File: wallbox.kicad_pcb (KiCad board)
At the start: 2 copper layers, 48 parts, among them J1 From Transformer, J2 To Wallbox, J3 UART, J4 Program, Q1 BC547, Q2 BC547, Q3 BC547, SW1 SW_Push, U1 KA78R33, U2 LM7805CT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

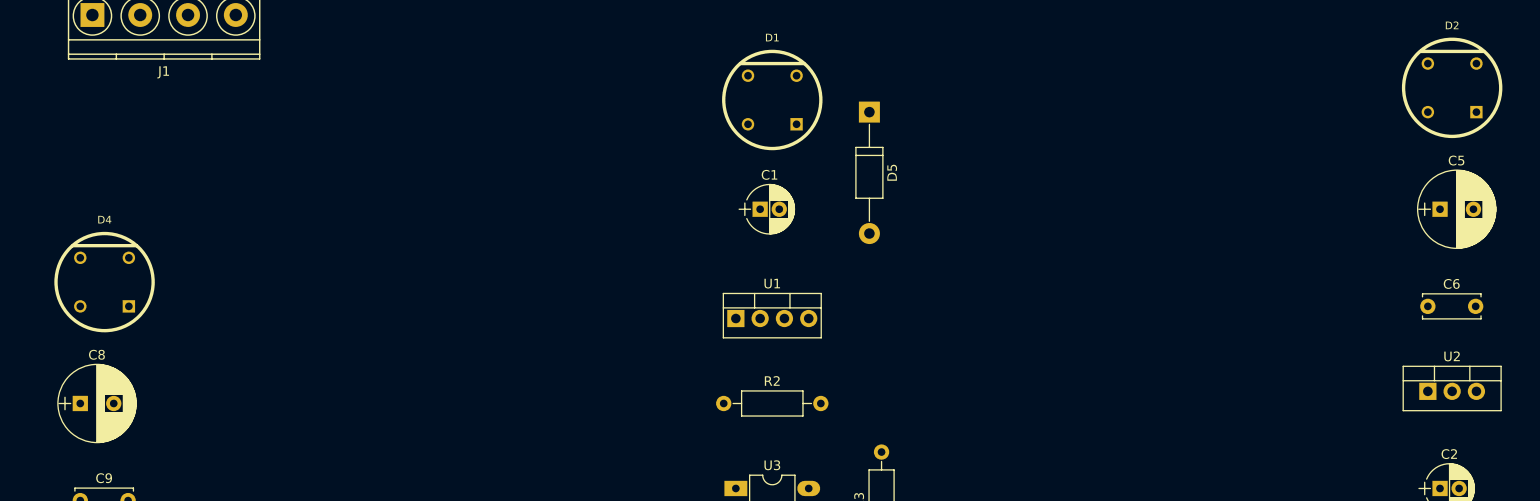
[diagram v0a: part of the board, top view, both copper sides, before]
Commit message: Fix WOG footprint pin numbering
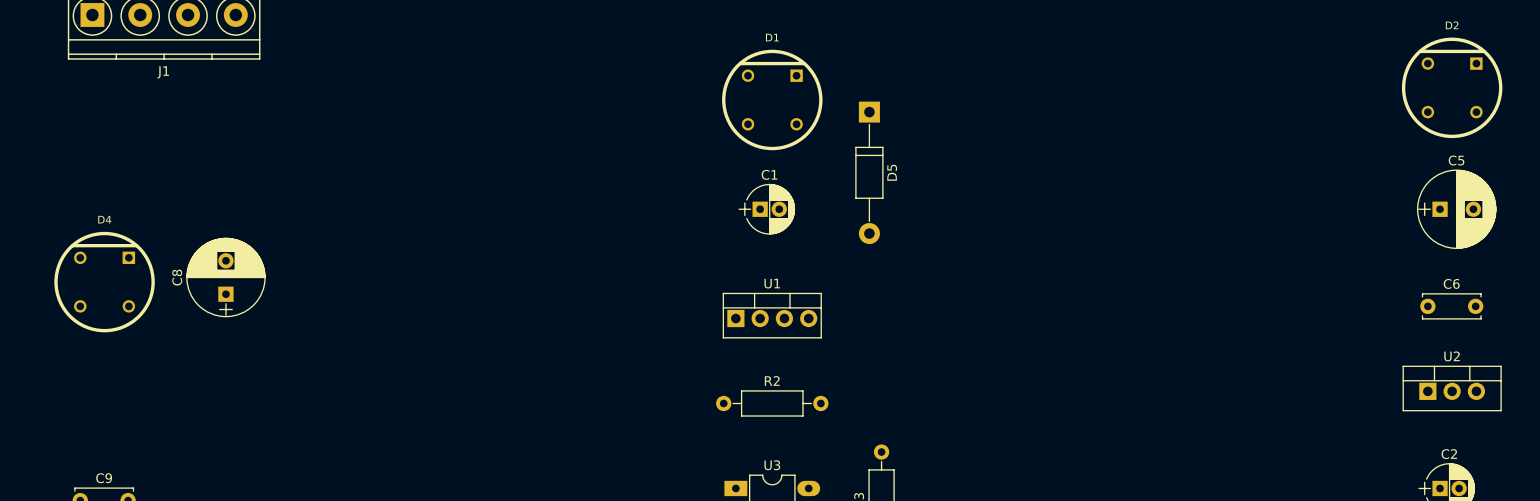
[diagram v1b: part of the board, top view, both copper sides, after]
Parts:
- moved C8 19.1 mm to (44.5, 78.7), turned to 90 degrees
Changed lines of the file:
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@@
   )
   (module Capacitors_THT:CP_Radial_D8.0mm_P3.50mm (layer F.Cu)
-    (at 29.21 90.17)
+    (at 44.45 78.74 90)
     (descr "CP, Radial series, Radial, pin pitch=3.50mm, , diameter=8mm, Electrolytic Capacitor")
     (tags "CP Radial series Radial pin pitch 3.50mm  diameter 8mm Electrolytic Capacitor")
-    (fp_text reference C8 (at 1.75 -5.06) (layer F.SilkS)
-      (effects (font (size 1 1) (thickness 0.15)))
-    )
-    (fp_text value 100uF (at 1.75 5.06) (layer F.Fab)
+    (fp_text reference C8 (at 1.75 -5.06 90) (layer F.SilkS)
+      (effects (font (size 1 1) (thickness 0.15)))
+    )
+    (fp_text value 100uF (at 1.75 5.06 90) (layer F.Fab)
       (effects (font (size 1 1) (thickness 0.15)))
     )
@@
     (fp_line (start 6.1 4.35) (end 6.1 -4.35) (layer F.CrtYd) (width 0.05))
     (fp_line (start 6.1 -4.35) (end -2.6 -4.35) (layer F.CrtYd) (width 0.05))
-    (pad 1 thru_hole rect (at 0 0) (size 1.6 1.6) (drill 0.8) (layers *.Cu *.Mask)
+    (pad 1 thru_hole rect (at 0 0 90) (size 1.6 1.6) (drill 0.8) (layers *.Cu *.Mask)
       (net 9 "Net-(C8-Pad1)"))
-    (pad 2 thru_hole circle (at 3.5 0) (size 1.6 1.6) (drill 0.8) (layers *.Cu *.Mask)
+    (pad 2 thru_hole circle (at 3.5 0 90) (size 1.6 1.6) (drill 0.8) (layers *.Cu *.Mask)
       (net 10 "Net-(C8-Pad2)"))
     (model Capacitors_THT.3dshapes/CP_Radial_D8.0mm_P3.50mm.wrl
@@
     (fp_line (start -3.302 -3.81) (end 3.302 -3.81) (layer F.SilkS) (width 0.35))
     (fp_circle (center 0 0) (end 0 -5.08) (layer F.SilkS) (width 0.35))
-    (pad 1 thru_hole rect (at 2.54 2.54) (size 1.3 1.3) (drill 0.8) (layers *.Cu *.Mask F.SilkS)
+    (pad 2 thru_hole circle (at 2.54 2.54) (size 1.3 1.3) (drill 0.8) (layers *.Cu *.Mask F.SilkS)
+      (net 14 "Net-(D2-Pad2)"))
+    (pad 3 thru_hole circle (at -2.54 2.54) (size 1.3 1.3) (drill 0.8) (layers *.Cu *.Mask F.SilkS)
+      (net 10 "Net-(C8-Pad2)"))
+    (pad 1 thru_hole rect (at 2.54 -2.54) (size 1.3 1.3) (drill 0.8) (layers *.Cu *.Mask F.SilkS)
       (net 9 "Net-(C8-Pad1)"))
-    (pad 2 thru_hole circle (at -2.54 2.54) (size 1.3 1.3) (drill 0.8) (layers *.Cu *.Mask F.SilkS)
-      (net 14 "Net-(D2-Pad2)"))
-    (pad 3 thru_hole circle (at 2.54 -2.54) (size 1.3 1.3) (drill 0.8) (layers *.Cu *.Mask F.SilkS)
-      (net 10 "Net-(C8-Pad2)"))
     (pad 4 thru_hole circle (at -2.54 -2.54) (size 1.3 1.3) (drill 0.8) (layers *.Cu *.Mask F.SilkS)
       (net 15 "Net-(D2-Pad4)"))
@@
     (fp_line (start -3.302 -3.81) (end 3.302 -3.81) (layer F.SilkS) (width 0.35))
     (fp_circle (center 0 0) (end 0 -5.08) (layer F.SilkS) (width 0.35))
-    (pad 1 thru_hole rect (at 2.54 2.54) (size 1.3 1.3) (drill 0.8) (layers *.Cu *.Mask F.SilkS)
+    (pad 2 thru_hole circle (at 2.54 2.54) (size 1.3 1.3) (drill 0.8) (layers *.Cu *.Mask F.SilkS)
+      (net 12 "Net-(D1-Pad2)"))
+    (pad 3 thru_hole circle (at -2.54 2.54) (size 1.3 1.3) (drill 0.8) (layers *.Cu *.Mask F.SilkS)
+      (net 2 "Net-(C1-Pad2)"))
+    (pad 1 thru_hole rect (at 2.54 -2.54) (size 1.3 1.3) (drill 0.8) (layers *.Cu *.Mask F.SilkS)
       (net 11 "Net-(D1-Pad1)"))
-    (pad 2 thru_hole circle (at -2.54 2.54) (size 1.3 1.3) (drill 0.8) (layers *.Cu *.Mask F.SilkS)
-      (net 12 "Net-(D1-Pad2)"))
-    (pad 3 thru_hole circle (at 2.54 -2.54) (size 1.3 1.3) (drill 0.8) (layers *.Cu *.Mask F.SilkS)
-      (net 2 "Net-(C1-Pad2)"))
     (pad 4 thru_hole circle (at -2.54 -2.54) (size 1.3 1.3) (drill 0.8) (layers *.Cu *.Mask F.SilkS)
       (net 13 "Net-(D1-Pad4)"))
@@
     (fp_line (start -3.302 -3.81) (end 3.302 -3.81) (layer F.SilkS) (width 0.35))
     (fp_circle (center 0 0) (end 0 -5.08) (layer F.SilkS) (width 0.35))
-    (pad 1 thru_hole rect (at 2.54 2.54) (size 1.3 1.3) (drill 0.8) (layers *.Cu *.Mask F.SilkS)
+    (pad 2 thru_hole circle (at 2.54 2.54) (size 1.3 1.3) (drill 0.8) (layers *.Cu *.Mask F.SilkS)
+      (net 14 "Net-(D2-Pad2)"))
+    (pad 3 thru_hole circle (at -2.54 2.54) (size 1.3 1.3) (drill 0.8) (layers *.Cu *.Mask F.SilkS)
+      (net 4 "Net-(C2-Pad2)"))
+    (pad 1 thru_hole rect (at 2.54 -2.54) (size 1.3 1.3) (drill 0.8) (layers *.Cu *.Mask F.SilkS)
       (net 8 "Net-(C5-Pad1)"))
-    (pad 2 thru_hole circle (at -2.54 2.54) (size 1.3 1.3) (drill 0.8) (layers *.Cu *.Mask F.SilkS)
-      (net 14 "Net-(D2-Pad2)"))
-    (pad 3 thru_hole circle (at 2.54 -2.54) (size 1.3 1.3) (drill 0.8) (layers *.Cu *.Mask F.SilkS)
-      (net 4 "Net-(C2-Pad2)"))
     (pad 4 thru_hole circle (at -2.54 -2.54) (size 1.3 1.3) (drill 0.8) (layers *.Cu *.Mask F.SilkS)
       (net 15 "Net-(D2-Pad4)"))

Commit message: Routed some elements
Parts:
- moved D3 67.1 mm to (229.9, 92.7), turned to 270 degrees
- moved C6 53.5 mm to (223.5, 76.2), turned to 270 degrees
- moved C7 52.2 mm to (222.2, 102.9), turned to 180 degrees
- moved C2 49.6 mm to (221.0, 96.5), turned to 180 degrees
- moved U2 45.7 mm to (215.9, 88.9)
- moved R9 44.5 mm to (227.3, 121.9), turned to 270 degrees
- moved C5 42.4 mm to (213.4, 76.2), turned to 270 degrees
- moved C9 36.0 mm to (53.3, 73.7), turned to 270 degrees
- moved D2 35.3 mm to (200.7, 78.7)
- moved U8 27.9 mm to (53.3, 88.9), turned to 270 degrees
- moved Q3 26.7 mm to (243.8, 124.5)
- moved J2 25.5 mm to (254.0, 44.5), turned to 90 degrees
- moved R7 25.0 mm to (217.2, 121.9), turned to 270 degrees
- moved U6 24.4 mm to (241.3, 135.9)
- moved R6 22.7 mm to (238.8, 130.8)
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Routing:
- net Net-(C2-Pad2): track 0.00 -> 173.1 mm, vias 0 -> 3
- net Net-(C2-Pad1): track 0.00 -> 150.3 mm
- net Net-(R7-Pad1): track 0.00 -> 51.4 mm
- net GND: track 0.00 -> 51.4 mm
- net Net-(C5-Pad1): track 0.00 -> 51.1 mm
- net Net-(C8-Pad1): track 0.00 -> 51.1 mm
- net Net-(C8-Pad2): track 0.00 -> 37.7 mm
- net Net-(Q2-Pad1): track 0.00 -> 28.2 mm
- net Net-(Q1-Pad1): track 0.00 -> 28.2 mm
- net Net-(Q3-Pad1): track 0.00 -> 28.2 mm
- net Net-(R9-Pad1): track 0.00 -> 26.5 mm
- net Net-(R8-Pad1): track 0.00 -> 25.7 mm
- net Net-(D2-Pad2): track 0.00 -> 22.9 mm
- net Net-(Q3-Pad2): track 0.00 -> 18.3 mm
- net Net-(Q2-Pad2): track 0.00 -> 18.3 mm
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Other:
- board text added: "10c"
- board text added: "25VAC"
- board text added: "25c"
- board text added: "5c"
- board text added: "Center"
- board text added: "Com"
- board text added: "GND"
- board text added: "Signal"

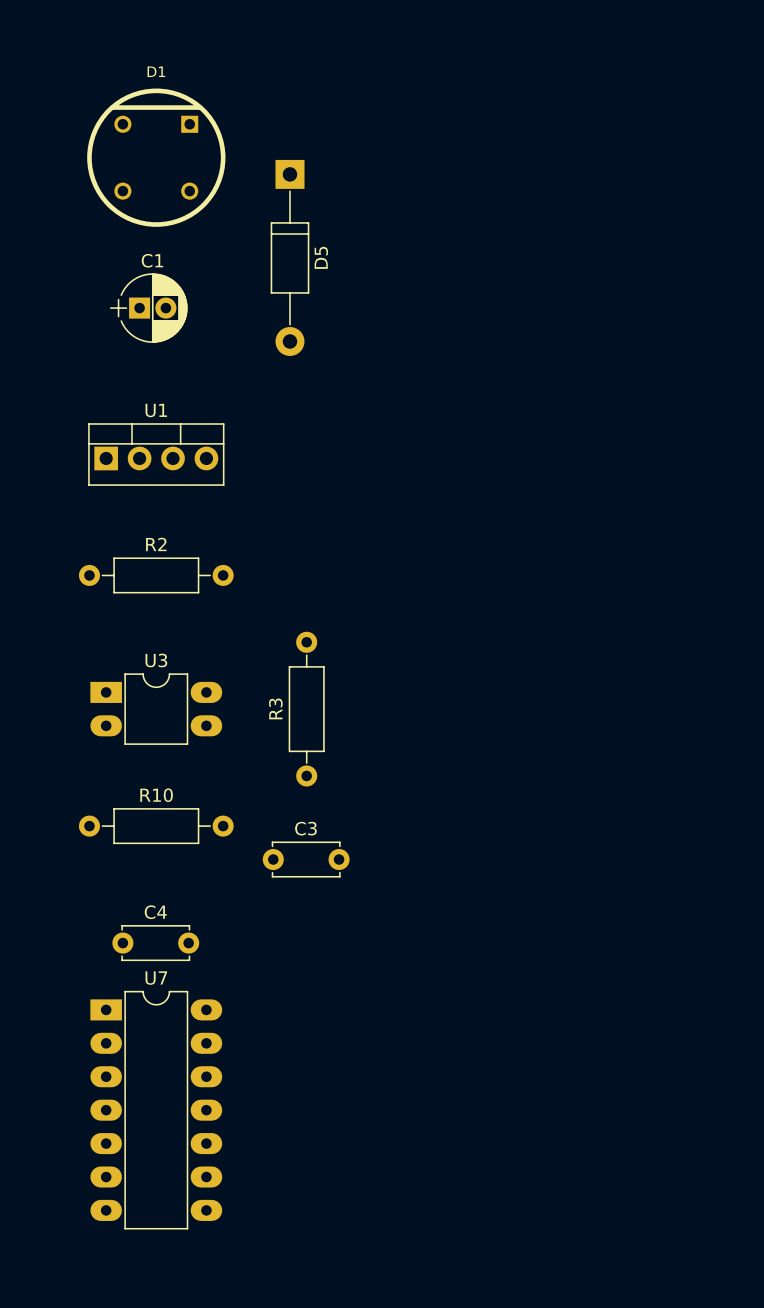
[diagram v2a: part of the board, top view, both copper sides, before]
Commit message: More submodules routed
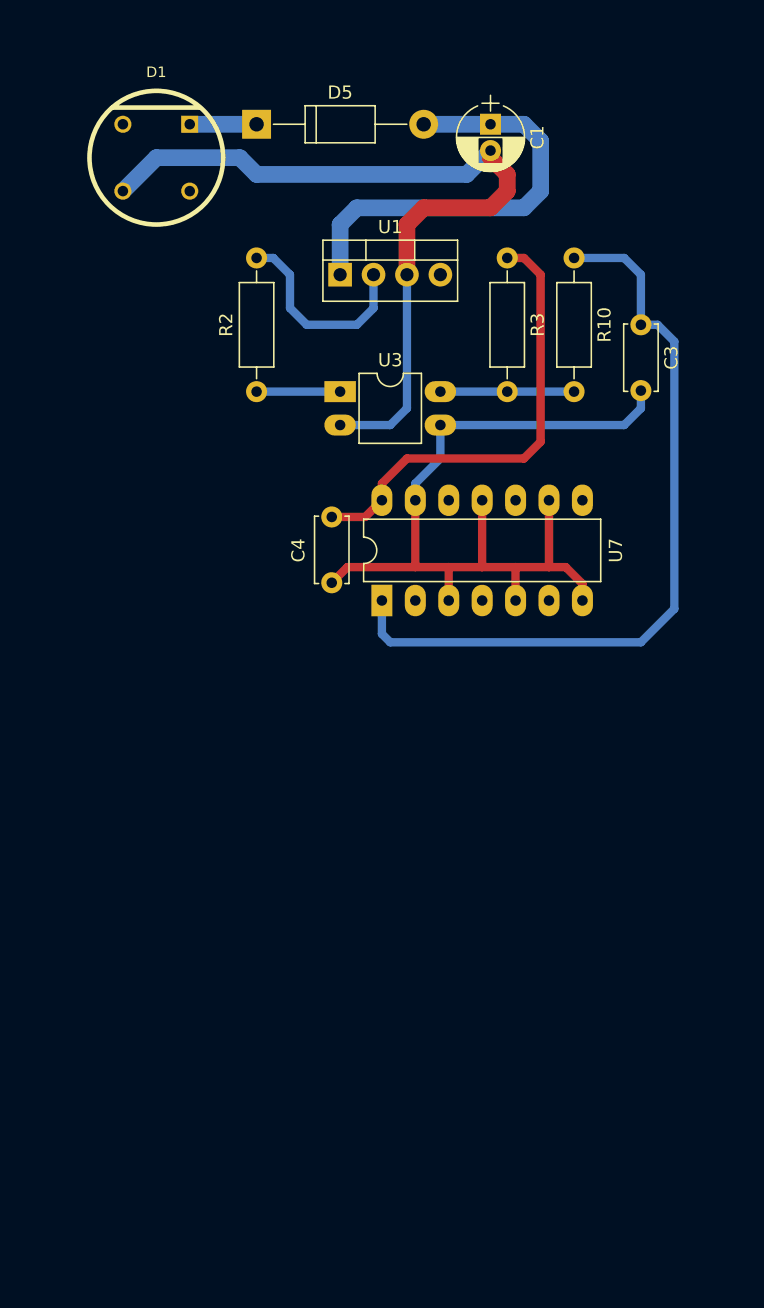
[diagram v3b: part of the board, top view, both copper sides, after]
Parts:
- C4: value 0.1uF -> 0.1
- moved R10 56.8 mm to (133.3, 66.0), turned to 270 degrees
- moved C3 49.3 mm to (138.4, 71.1), turned to 270 degrees
- moved R3 42.2 mm to (128.3, 66.0), turned to 270 degrees
- moved U7 37.5 mm to (118.7, 92.1), turned to 90 degrees
- moved C4 36.1 mm to (114.9, 85.7), turned to 270 degrees
- moved C1 30.1 mm to (127.0, 55.9), turned to 270 degrees
- moved U3 29.0 mm to (115.6, 76.2)
- moved U1 22.6 mm to (115.6, 67.3)
- moved R2 18.9 mm to (109.2, 76.2), turned to 90 degrees
- moved D5 4.58 mm to (109.2, 55.9), turned to 0 degrees
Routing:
- net GND: track 51.4 -> 116.7 mm
- net Net-(C1-Pad2): track 0.00 -> 62.1 mm
- net Net-(C3-Pad1): track 0.00 -> 58.9 mm
- net VCC: track 0.00 -> 34.8 mm
- net Net-(C1-Pad1): track 0.00 -> 33.3 mm
- net Net-(R2-Pad2): track 0.00 -> 15.5 mm
- net Net-(R10-Pad2): track 0.00 -> 10.2 mm
- net Net-(R2-Pad1): track 0.00 -> 6.35 mm
- net Net-(D1-Pad1): track 0.00 -> 5.08 mm

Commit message: Getting there, just need to rearrange and route logic power
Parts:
- moved SW1 102.8 mm to (63.5, 99.1)
- moved J4 98.0 mm to (19.1, 114.3)
- moved R12 97.4 mm to (35.6, 100.3), turned to 180 degrees
- moved J3 96.0 mm to (19.1, 100.3)
- moved R11 90.2 mm to (71.1, 109.2), turned to 180 degrees
- moved R14 84.1 mm to (25.4, 110.5)
- moved R13 81.8 mm to (25.4, 105.4)
- moved R1 81.1 mm to (71.1, 114.3), turned to 180 degrees
- moved U9 73.3 mm to (55.9, 114.3), turned to 180 degrees
- moved J2 8.89 mm to (254.0, 53.3)
- moved J1 1.27 mm to (29.2, 27.9)
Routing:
- net VCC: track 34.8 -> 133.2 mm
- net Net-(J3-Pad2): track 0.00 -> 44.2 mm
- net Net-(J3-Pad1): track 0.00 -> 35.3 mm
- net GND: track 116.7 -> 148.2 mm
- net Net-(J4-Pad1): track 0.00 -> 29.7 mm
- net Net-(R1-Pad2): track 0.00 -> 23.4 mm
- net Net-(R12-Pad1): track 0.00 -> 7.21 mm
- net Net-(R13-Pad2): track 0.00 -> 6.78 mm
- net Net-(R11-Pad2): track 0.00 -> 5.53 mm

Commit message: More progress, added board outline
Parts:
- added REF**: 1pin, wallbox-footprints:1pin_hole, F.Cu at (15.9, 15.9)
- added REF**: 1pin, wallbox-footprints:1pin_hole, F.Cu at (174.6, 15.9)
- added REF**: 1pin, wallbox-footprints:1pin_hole, F.Cu at (174.6, 102.9)
- added REF**: 1pin, wallbox-footprints:1pin_hole, F.Cu at (15.9, 102.9)
- C4: value 0.1 -> 0.1uF
- moved C5 121.7 mm to (101.6, 27.9)
- moved R9 121.7 mm to (115.6, 73.7)
- moved RL1 121.7 mm to (143.5, 29.2)
- moved RL2 121.7 mm to (143.5, 52.1)
- moved RL3 121.7 mm to (143.5, 74.9)
- moved U4 121.7 mm to (129.5, 41.9)
- moved U5 121.7 mm to (129.5, 64.8)
- moved U6 121.7 mm to (129.5, 87.6)
- moved C6 121.7 mm to (111.8, 27.9)
- moved C7 121.7 mm to (110.5, 54.6)
- moved D3 121.7 mm to (118.1, 44.5)
- moved R8 121.7 mm to (110.5, 73.7)
- moved U2 121.7 mm to (104.1, 40.6)
- moved C2 121.7 mm to (109.2, 48.3)
- moved D2 121.7 mm to (88.9, 30.5)
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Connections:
- J2 pad 1: Net-(D1-Pad2) -> Net-(J2-Pad1)
- J2 pad 2: Net-(D1-Pad4) -> Net-(J2-Pad2)
- J2 pad 3: Net-(D2-Pad2) -> Net-(J2-Pad3)
- J2 pad 4: Net-(J2-Pad4) -> Net-(D2-Pad2)
- J2 pad 5: Net-(J2-Pad5) -> Net-(D1-Pad4)
- J2 pad 6: Net-(J2-Pad6) -> Net-(D1-Pad2)
- RL1 pad 1: Net-(J2-Pad4) -> Net-(J2-Pad3)
- RL1 pad 14: Net-(J2-Pad4) -> Net-(J2-Pad3)
- RL2 pad 1: Net-(J2-Pad5) -> Net-(J2-Pad2)
- RL2 pad 14: Net-(J2-Pad5) -> Net-(J2-Pad2)
- RL3 pad 1: Net-(J2-Pad6) -> Net-(J2-Pad1)
- RL3 pad 14: Net-(J2-Pad6) -> Net-(J2-Pad1)
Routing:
- net Net-(D2-Pad2): track 22.9 -> 298.1 mm
- net Net-(D1-Pad4): track 0.00 -> 171.7 mm, vias 0 -> 1
- net Net-(D1-Pad2): track 0.00 -> 126.7 mm, vias 0 -> 2
- net Net-(D2-Pad4): track 0.00 -> 110.1 mm
- net Net-(J2-Pad1): track 0.00 -> 42.4 mm
- net Net-(J2-Pad3): track 0.00 -> 33.8 mm
- net Net-(J2-Pad2): track 0.00 -> 23.1 mm
- net Net-(J2-Pad6): track 7.62 -> 0.00 mm
- net Net-(J2-Pad5): track 7.62 -> 0.00 mm
- net Net-(J2-Pad4): track 7.62 -> 0.00 mm
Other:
- board outline added: 166.4 x 94.6 mm
- board text added: "+V"
- board text added: "RX"
- board text added: "TX"
